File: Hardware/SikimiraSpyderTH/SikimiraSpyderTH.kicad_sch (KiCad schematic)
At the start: 39 parts, among them U1 ESP32_DevKit_V1_DOIT, U3 AMS1117-5.0

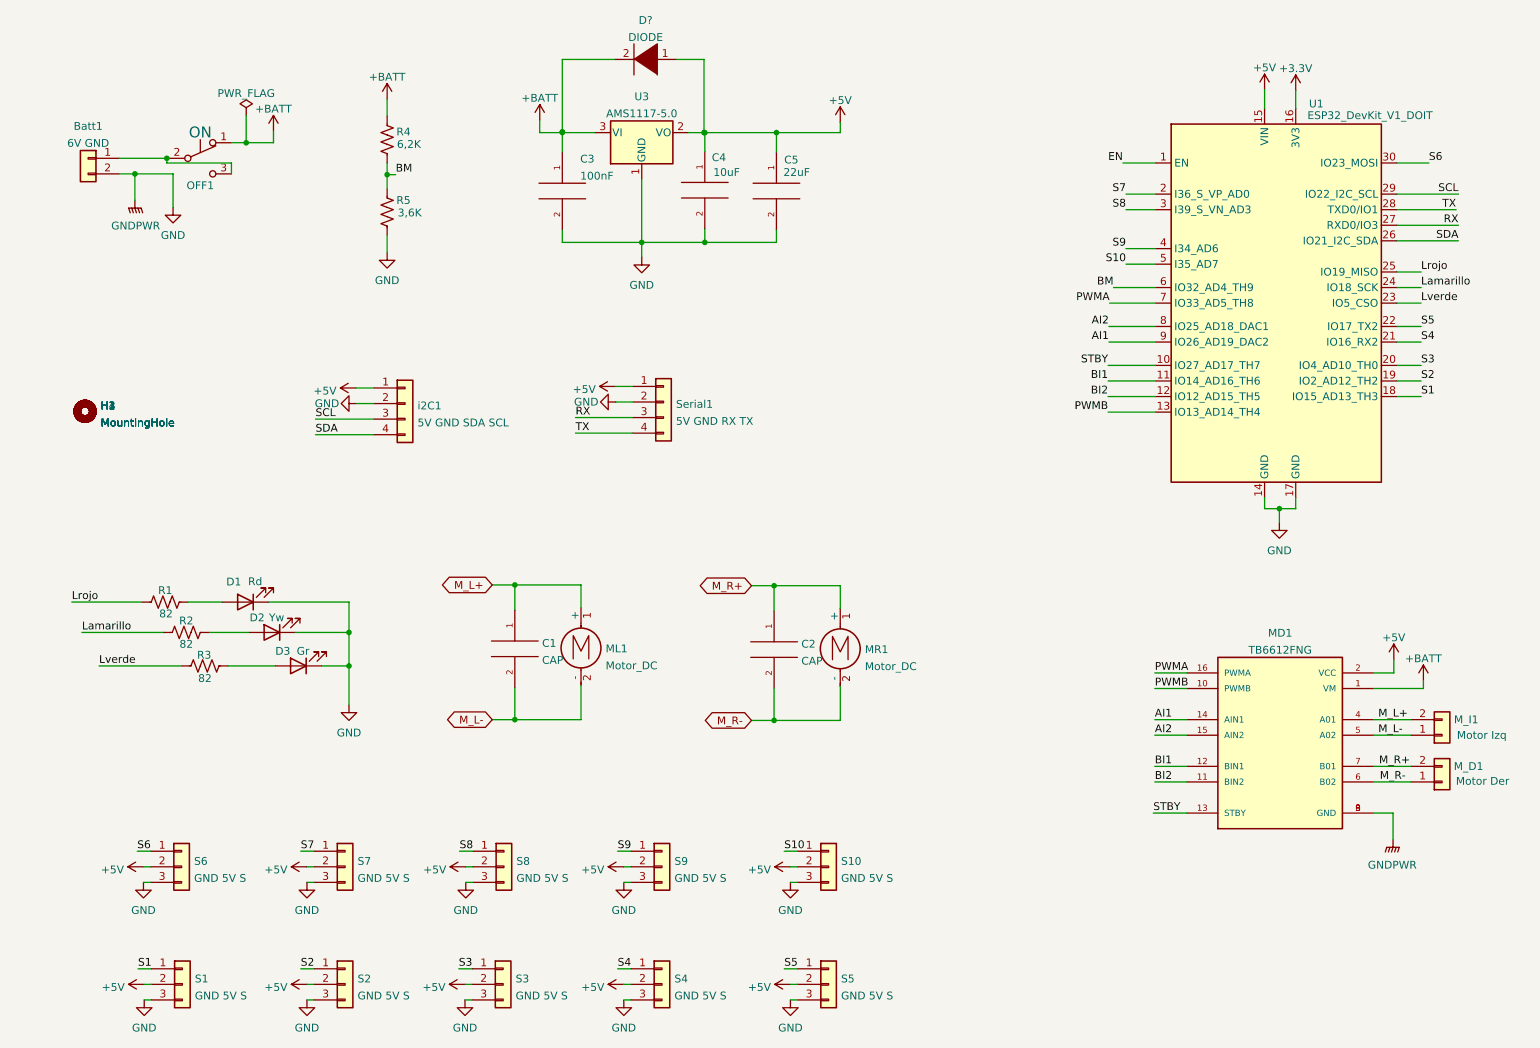
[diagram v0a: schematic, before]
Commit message: PCB Creada, Cambio de pines
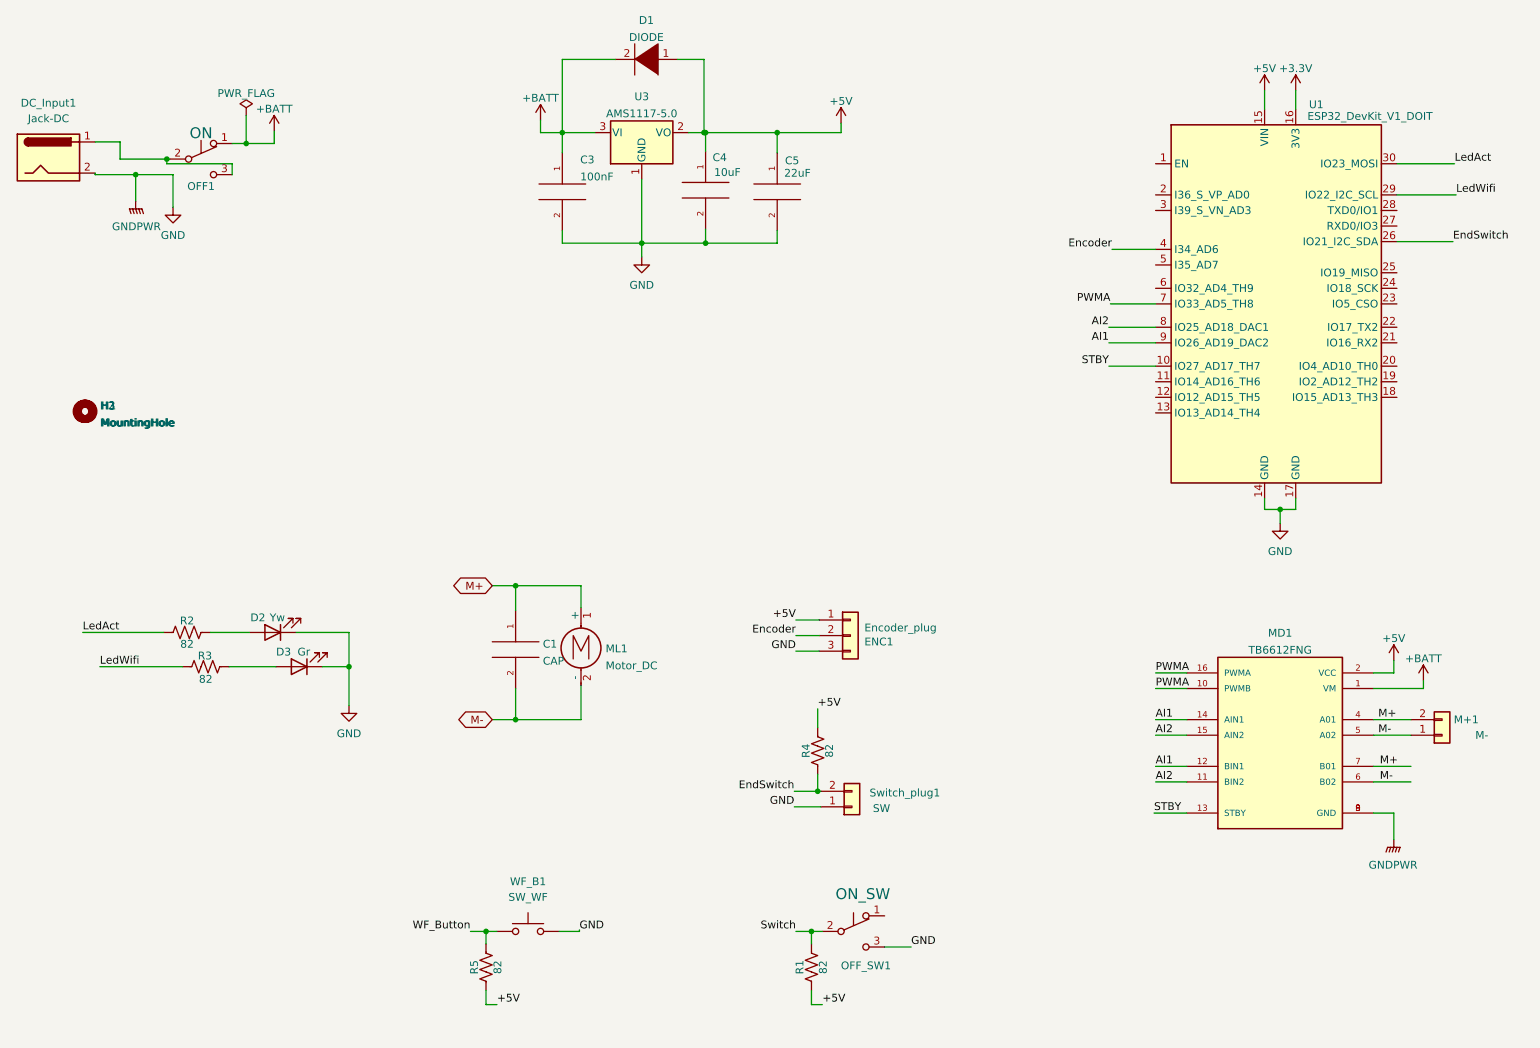
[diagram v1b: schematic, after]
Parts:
- removed Batt1: 6V GND, Connector_JST:JST_PH_B2B-PH-K_1x02_P2.00mm_Vertical, symbol Connector_Generic:Conn_01x02
- removed C2: CAP, Capacitor_THT:C_Disc_D3.0mm_W2.0mm_P2.50mm, symbol pspice:CAP
- removed D1: Rd, LED_THT:LED_D5.0mm, symbol Device:LED
- removed H4: MountingHole, MountingHole:MountingHole_3.2mm_M3_ISO7380_Pad, symbol Mechanical:MountingHole
- removed MR1: Motor_DC, NetTie:NetTie-2_SMD_Pad0.5mm, symbol Motor:Motor_DC
- removed M_D1: Motor Der, Connector_JST:JST_PH_B2B-PH-K_1x02_P2.00mm_Vertical, symbol Connector_Generic:Conn_01x02
- removed S1, S10, S2, S3, S4, S5, S6, S7, S8, S9: GND 5V S, Connector_PinHeader_2.54mm:PinHeader_1x03_P2.54mm_Vertical, symbol Connector_Generic:Conn_01x03
- removed Serial1: 5V GND RX TX, Connector_PinHeader_2.54mm:PinHeader_1x04_P2.54mm_Vertical, symbol Connector_Generic:Conn_01x04
- removed i2C1: 5V GND SDA SCL, Connector_PinHeader_2.54mm:PinHeader_1x04_P2.54mm_Vertical, symbol Connector_Generic:Conn_01x04
- added DC_Input1: Jack-DC, Connector_BarrelJack:BarrelJack_Horizontal, symbol Connector:Jack-DC
- added ENC1: Encoder_plug, Connector_JST:JST_EH_B3B-EH-A_1x03_P2.50mm_Vertical, symbol Connector_Generic:Conn_01x03
- added OFF_SW1: ON_SW, Button_Switch_THT:SW_Slide_1P2T_CK_OS102011MS2Q, symbol Switch:SW_Push_SPDT
- added Switch_plug1: SW, Connector_JST:JST_PH_B2B-PH-K_1x02_P2.00mm_Vertical, symbol Connector_Generic:Conn_01x02
- added WF_B1: SW_WF, Button_Switch_THT:SW_Tactile_SPST_Angled_PTS645Vx39-2LFS, symbol Switch:SW_Push
- D1: renamed from D?; footprint (none) -> Diode_SMD:D_0805_2012Metric_Pad1.15x1.40mm_HandSolder
- M+1: renamed from M_I1; value Motor Izq -> M-
- MD1: footprint TB6612FNG Motor:MODULE_TB6612FNG Motor -> TB6612FNG:MODULE_TB6612FNG Motor
- R4: value 6,2K -> 82; footprint Resistor_SMD:R_1206_3216Metric -> Resistor_THT:R_Axial_DIN0207_L6.3mm_D2.5mm_P10.16mm_Horizontal
- R5: value 3,6K -> 82; footprint Resistor_SMD:R_1206_3216Metric -> Resistor_THT:R_Axial_DIN0207_L6.3mm_D2.5mm_P10.16mm_Horizontal
- U1: footprint esp32_devkit_v1_doit:esp32_devkit_v1_doit -> ESP32_30PIN:esp32_devkit_v1_doit
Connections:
- net M_R+ is gone; now on net M+: MD1.7 (B01)
- net M_R- is gone; now on net M-: MD1.6 (B02)
- net +5V: now also R1.1, R4.2, R5.1, ENC1.1 (Pin_1)
- net +BATT: now also D1.2 (A); no longer R4.2
- net AI1: now also MD1.12 (BIN1)
- net AI2: now also MD1.11 (BIN2)
- net GND: now also DC_Input1.2, ENC1.3 (Pin_3), OFF_SW1.3 (C), Switch_plug1.1 (Pin_1), WF_B1.2; no longer R5.1
- net PWMA: now also MD1.10 (PWMB)
- net Switch: now reaches R1.2
- net Switch: now also OFF_SW1.2 (B)
- net at OFF1.2 (B), OFF1.3 (C): now also DC_Input1.1
- net BI1: no longer names the net of U1.11 (IO14_AD16_TH6)
- net BI1: no longer MD1.12 (BIN1)
- net BI2: no longer names the net of U1.12 (IO12_AD15_TH5)
- net BI2: no longer MD1.11 (BIN2)
- removed net BM: R4.1, R5.2, U1.6 (IO32_AD4_TH9)
- net EN: no longer names the net of U1.1 (EN)
- net Lamarillo: no longer names the net of U1.24 (IO18_SCK)
- net Lamarillo: no longer R2.1
- net Lrojo: no longer names the net of U1.25 (IO19_MISO)
- net Lrojo: no longer R1.1
- net Lverde: no longer names the net of U1.23 (IO5_CSO)
- net Lverde: no longer R3.1
- net M_L+ renamed M+
- net M_L- renamed M-
- net PWMB: no longer names the net of U1.13 (IO13_AD14_TH4)
- net PWMB: no longer MD1.10 (PWMB)
- net RX: no longer names the net of U1.27 (RXD0/IO3)
- net S1: no longer names the net of U1.18 (IO15_AD13_TH3)
- net S10: no longer names the net of U1.5 (I35_AD7)
- net S2: no longer names the net of U1.19 (IO2_AD12_TH2)
- net S3: no longer names the net of U1.20 (IO4_AD10_TH0)
- net S4: no longer names the net of U1.21 (IO16_RX2)
- net S5: no longer names the net of U1.22 (IO17_TX2)
- net S6 renamed LedAct
- net LedAct: now also R2.1
- net S7: no longer names the net of U1.2 (I36_S_VP_AD0)
- net S8: no longer names the net of U1.3 (I39_S_VN_AD3)
- net S9 renamed Encoder
- net Encoder: now also ENC1.2 (Pin_2)
- net SCL renamed LedWifi
- net LedWifi: now also R3.1
- net SDA renamed EndSwitch
- net EndSwitch: now also R4.1, Switch_plug1.2 (Pin_2)
- net TX: no longer names the net of U1.28 (TXD0/IO1)
- new net WF_Button: R5.2, WF_B1.1

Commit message: Cambiado de pines y corregido PCB
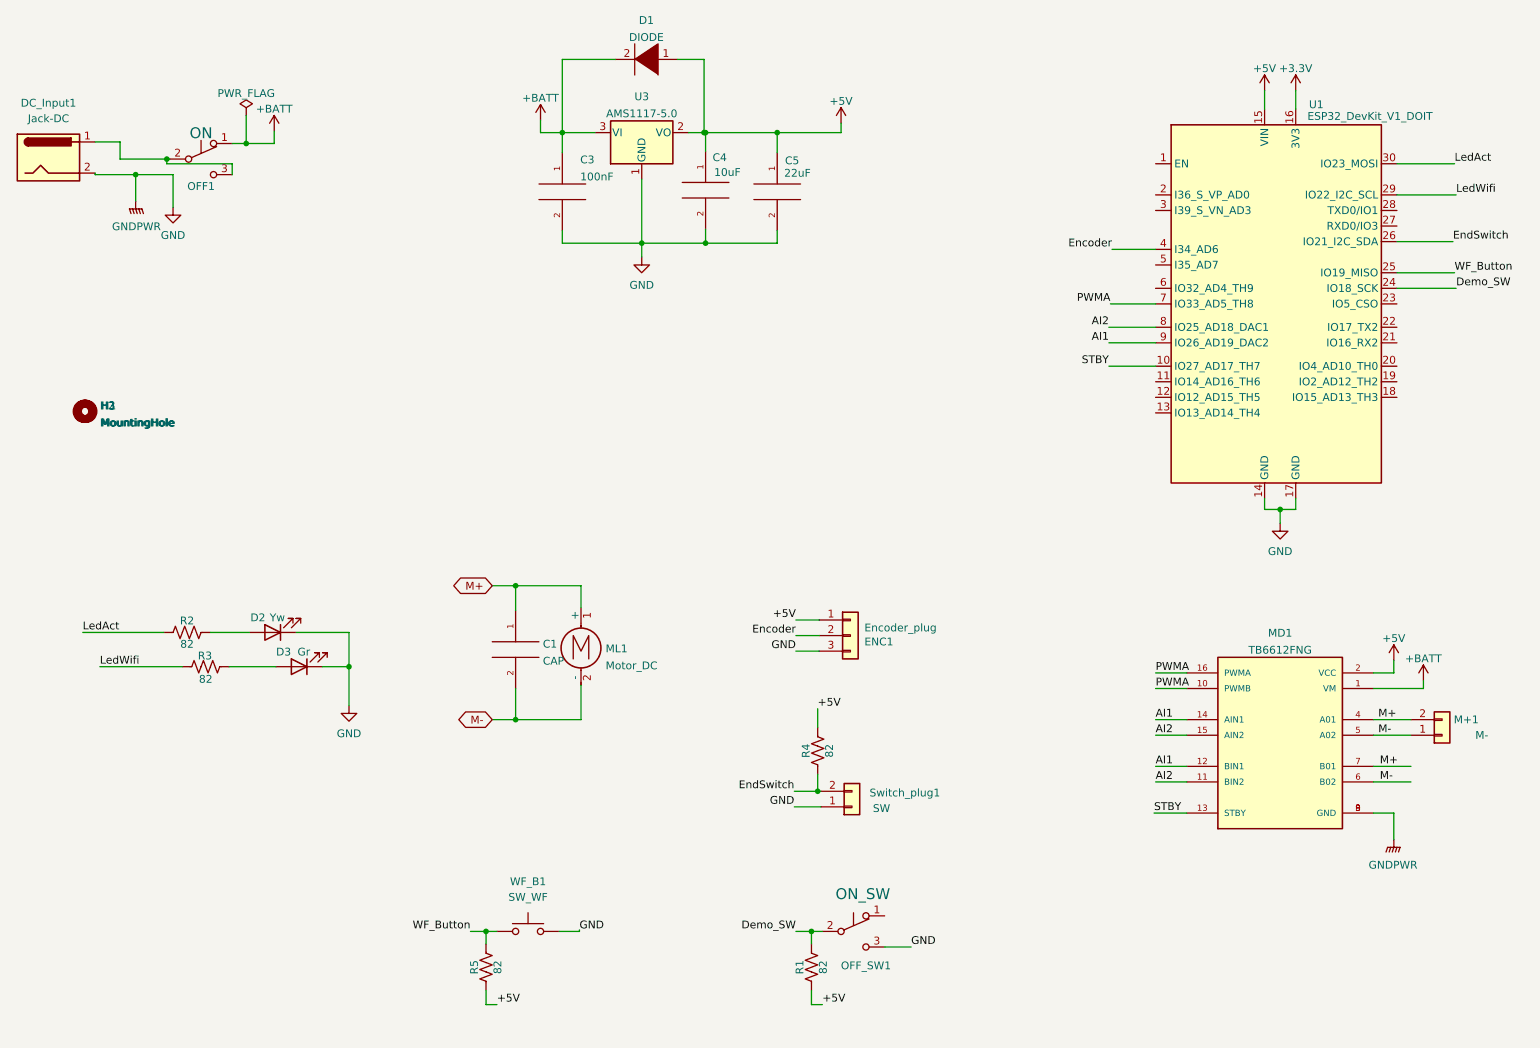
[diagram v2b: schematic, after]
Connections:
- net Switch is gone; now on net Demo_SW: OFF_SW1.2 (B), R1.2
- net WF_Button: now also U1.25 (IO19_MISO)
- net Demo_SW: now reaches U1.24 (IO18_SCK)
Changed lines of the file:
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@@
+    (stroke (width 0) (type default) (color 0 0 0 0))
+  )
+  (wire (pts (xy 243.332 59.436) (xy 252.984 59.436))
     (stroke (width 0) (type default) (color 0 0 0 0))
   )
@@
   )
   (wire (pts (xy 35.052 35.56) (xy 35.052 38.354))
+    (stroke (width 0) (type default) (color 0 0 0 0))
+  )
+  (wire (pts (xy 243.332 56.896) (xy 252.73 56.896))
     (stroke (width 0) (type default) (color 0 0 0 0))
   )
@@
     (effects (font (size 1.27 1.27)) (justify left bottom))
   )
-  (label "Switch" (at 145.288 164.338 180)
+  (label "Demo_SW" (at 145.288 164.338 180)
     (effects (font (size 1.27 1.27)) (justify right bottom))
   )
@@
     (effects (font (size 1.27 1.27)) (justify left bottom))
   )
+  (label "Demo_SW" (at 252.984 59.436 0)
+    (effects (font (size 1.27 1.27)) (justify left bottom))
+  )
   (label "LedAct" (at 252.73 39.116 0)
     (effects (font (size 1.27 1.27)) (justify left bottom))
@@
     (effects (font (size 1.27 1.27)) (justify right bottom))
   )
+  (label "WF_Button" (at 252.73 56.896 0)
+    (effects (font (size 1.27 1.27)) (justify left bottom))
+  )
   (label "M+" (at 240.538 137.414 0)

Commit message: Pcbs Update
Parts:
- M+1: footprint Connector_JST:JST_PH_B2B-PH-K_1x02_P2.00mm_Vertical -> TerminalBlock:TerminalBlock_bornier-2_P5.08mm
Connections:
- net Encoder: now also U1.11 (IO14_AD16_TH6); no longer U1.4 (I34_AD6)
- net GND: now also WF_B1.1; no longer WF_B1.2
- net WF_Button: now also WF_B1.2; no longer WF_B1.1
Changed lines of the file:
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@@
-    (stroke (width 0) (type default) (color 0 0 0 0))
-  )
-  (wire (pts (xy 196.85 53.086) (xy 203.962 53.086))
     (stroke (width 0) (type default) (color 0 0 0 0))
   )
@@
   )
   (wire (pts (xy 145.034 141.478) (xy 148.844 141.478))
+    (stroke (width 0) (type default) (color 0 0 0 0))
+  )
+  (wire (pts (xy 196.85 74.676) (xy 203.962 74.676))
     (stroke (width 0) (type default) (color 0 0 0 0))
   )
@@
     (effects (font (size 1.27 1.27)) (justify left bottom))
   )
+  (label "Encoder" (at 196.85 74.676 180)
+    (effects (font (size 1.27 1.27)) (justify right bottom))
+  )
   (label "AI1" (at 203.962 129.794 0)
     (effects (font (size 1.27 1.27)) (justify left bottom))
@@
   (label "AI2" (at 203.962 139.954 0)
     (effects (font (size 1.27 1.27)) (justify left bottom))
-  )
-  (label "Encoder" (at 196.85 53.086 180)
-    (effects (font (size 1.27 1.27)) (justify right bottom))
   )
   (label "WF_Button" (at 252.73 56.896 0)
@@
     (pin "2")
   )
+  (symbol (lib_id "Switch:SW_Push") (at 101.6 164.338 0) (mirror y) (unit 1)
+    (in_bom yes) (on_board yes) (fields_autoplaced)
+    (property "Reference" "WF_B1" (id 0) (at 101.6 156.718 0))
+    (property "Value" "SW_WF" (id 1) (at 101.6 159.258 0))
+    (property "Footprint" "Button_Switch_THT:SW_Tactile_SPST_Angled_PTS645Vx39-2LFS" (id 2) (at 101.6 159.258 0)
+      (effects (font (size 1.27 1.27)) hide)
+    )
+    (property "Datasheet" "~" (id 3) (at 101.6 159.258 0)
+      (effects (font (size 1.27 1.27)) hide)
+    )
+    (pin "1")
+    (pin "2")
+  )
   (symbol (lib_id "power:+BATT") (at 60.198 33.782 0) (mirror y) (unit 1)
     (in_bom yes) (on_board yes) (fields_autoplaced)
@@
     (property "Reference" "M+1" (id 0) (at 254.635 129.794 0))
     (property "Value" "M-" (id 1) (at 257.175 132.334 0))
-    (property "Footprint" "Connector_JST:JST_PH_B2B-PH-K_1x02_P2.00mm_Vertical" (id 2) (at 250.698 132.334 0)
+    (property "Footprint" "TerminalBlock:TerminalBlock_bornier-2_P5.08mm" (id 2) (at 250.698 132.334 0)
       (effects (font (size 1.27 1.27)) hide)
     )
@@
     (pin "1")
   )
-  (symbol (lib_id "Switch:SW_Push") (at 101.6 164.338 0) (unit 1)
-    (in_bom yes) (on_board yes) (fields_autoplaced)
-    (property "Reference" "WF_B1" (id 0) (at 101.6 156.21 0))
-    (property "Value" "SW_WF" (id 1) (at 101.6 158.75 0))
-    (property "Footprint" "Button_Switch_THT:SW_Tactile_SPST_Angled_PTS645Vx39-2LFS" (id 2) (at 101.6 159.258 0)
-      (effects (font (size 1.27 1.27)) hide)
-    )
-    (property "Datasheet" "~" (id 3) (at 101.6 159.258 0)
-      (effects (font (size 1.27 1.27)) hide)
-    )
-    (pin "1")
-    (pin "2")
-  )
   (symbol (lib_id "pspice:CAP") (at 107.188 43.688 0) (unit 1)
     (in_bom yes) (on_board yes)
@@
     )
     (path "/3a7fcad4-491e-4c6f-b408-d3bdedc76fd0"
-      (reference "M+1") (unit 1) (value "M-") (footprint "Connector_JST:JST_PH_B2B-PH-K_1x02_P2.00mm_Vertical")
+      (reference "M+1") (unit 1) (value "M-") (footprint "TerminalBlock:TerminalBlock_bornier-2_P5.08mm")
     )
     (path "/bf8196c3-4c84-43d9-b281-2fd3045968e7"
@@
       (reference "U3") (unit 1) (value "AMS1117-5.0") (footprint "Package_TO_SOT_SMD:SOT-223-3_TabPin2")
     )
-    (path "/73065c22-28cf-4e87-8ca1-286c49760392"
+    (path "/35f12dc4-2945-42f2-8dd7-2847ca46528c"
       (reference "WF_B1") (unit 1) (value "SW_WF") (footprint "Button_Switch_THT:SW_Tactile_SPST_Angled_PTS645Vx39-2LFS")
     )
